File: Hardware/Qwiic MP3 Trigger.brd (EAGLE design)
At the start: 25.4 x 50.8 mm, 106 parts, among them J14 MICRO-SD, J2 QWIIC_RIGHT_ANGLE, J3 PTH, J4 QWIIC_RIGHT_ANGLE, J7 ISP, J8 3.5mm Audio, J9 Poke-Home, U1 TPA2005D1, U2 MY1690-16S, U3 AP2112-3.3V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

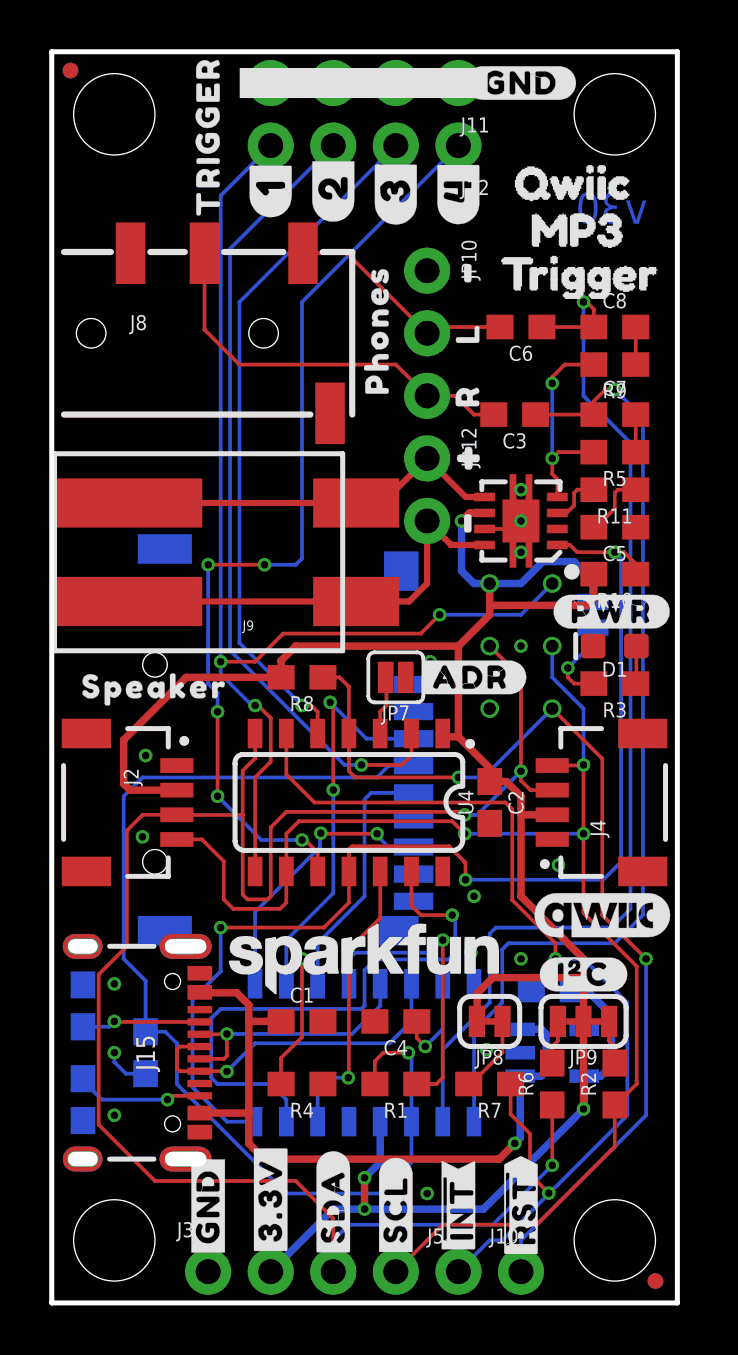
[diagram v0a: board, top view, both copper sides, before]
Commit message: Route MY1690X-16S
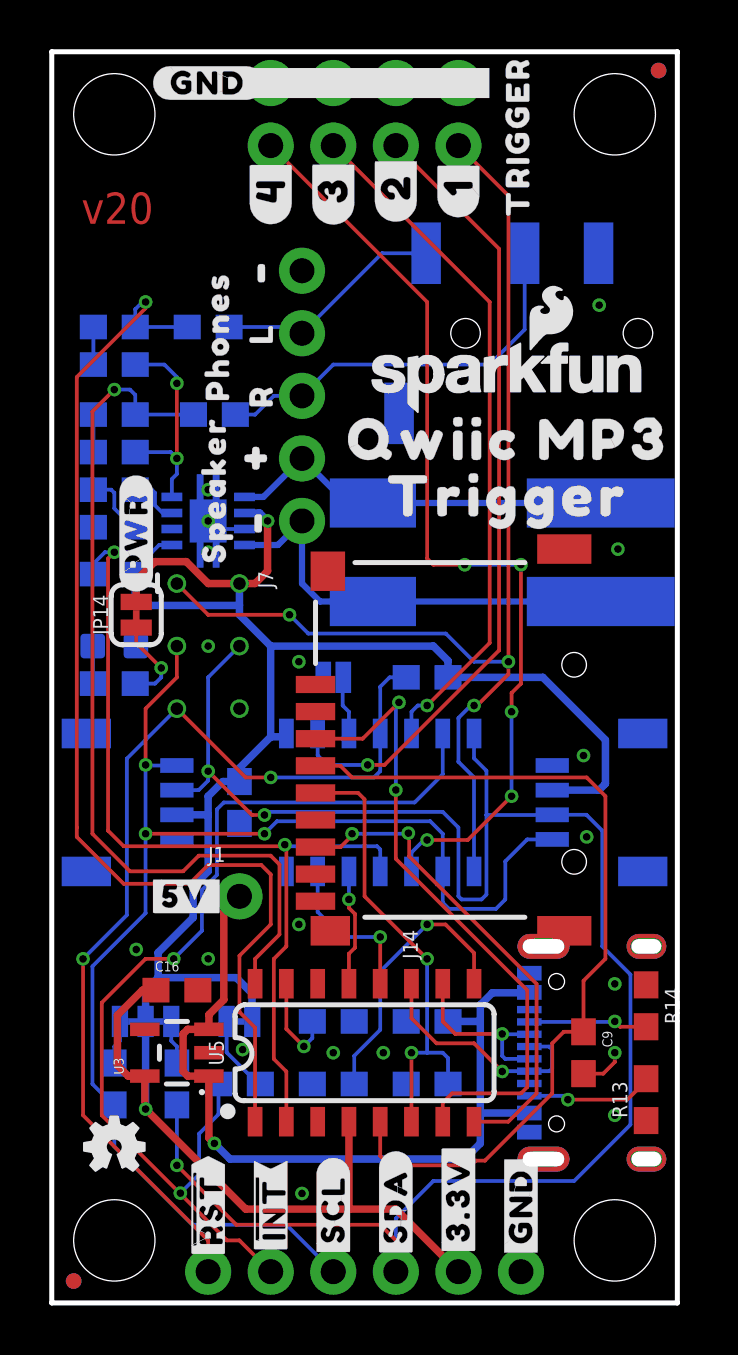
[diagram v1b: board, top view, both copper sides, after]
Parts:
- removed R1: 10k, SparkFun-Resistors:0603
- removed U2: MY1690-16S, MY1690:SO16
- added C10: 2.2uF, SparkFun-Capacitors:0603
- added J1: (no value), SparkFun-Connectors:1X01_NO_SILK
- added U$3: (no value), output:#5V#0
- added U5: MY1690X-16S, MY1690X-16S:SO16
- C4: value 1.0uF -> 2.2uF
- moved FRAME1 63.5 mm to (-19.1, -34.3), flipped to the top
- moved J8 25.4 mm to (25.4, 39.4), flipped to the bottom
- moved JP1 23.9 mm to (24.6, 50.0), flipped to the top
- moved JP6 23.9 mm to (24.6, 50.0), flipped to the bottom
- moved JP2 23.6 mm to (0.89, 0.89), flipped to the bottom
- moved JP5 23.6 mm to (0.89, 0.89), flipped to the top
- moved R13 22.9 mm to (24.1, 8.26), flipped to the top
- moved R14 22.9 mm to (24.1, 12.1), flipped to the top
- moved C5 20.3 mm to (2.54, 31.5), flipped to the bottom
- moved C7 20.3 mm to (2.54, 36.1), flipped to the bottom
- moved C8 20.3 mm to (2.54, 39.6), flipped to the bottom
- moved D1 20.3 mm to (2.54, 26.7), flipped to the bottom
- moved JP11 20.3 mm to (22.9, 2.54), flipped to the bottom
- moved JP13 20.3 mm to (2.54, 2.54), flipped to the bottom
- moved JP3 20.3 mm to (22.9, 48.3), flipped to the bottom
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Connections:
- removed net ADKEY: R1.1, U2.4
- new net N$10: C10.1, U5.9
- net 3.3V: now also U5.4; no longer U2.12
- net 5V: now also J1.1
- net D+: now also U5.11; no longer U2.6
- net D-: now also U5.10; no longer U2.5
- net GND: now also C10.2, U5.14, U5.3; no longer U2.13, U2.8
- net MP3-RXI: now also U5.12; no longer U2.15
- net MP3-TXO: now also U5.13; no longer U2.14
- net N$7: now also U5.15; no longer U2.7
- net PLAYING: now also U5.2; no longer U2.16
- net SD_CLK: now also U5.6; no longer U2.3
- net SD_CMD: now also U5.7; no longer U2.2
- net SD_DAT: now also U5.8; no longer U2.1
- net VCCIO: now also U5.5; no longer R1.2, U2.11
- net VOUTL: now also U5.16; no longer U2.9
- net VOUTR: now also U5.1; no longer U2.10
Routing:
- net MP3-RXI: track 23.4 -> 6.50 mm
- net ADKEY: track 11.9 -> 0.00 mm, vias 1 -> 0
- net N$10: track 0.00 -> 11.3 mm, vias 0 -> 1
- net SD_CMD: track 16.3 -> 26.3 mm
- net VCCIO: track 44.1 -> 35.5 mm, vias 1 -> 0
- net SD_DAT: track 11.3 -> 19.8 mm
- net PLAYING: track 46.8 -> 39.3 mm, vias 3 -> 2
- net MP3-TXO: track 11.6 -> 4.76 mm
- net 5V: track 29.1 -> 35.0 mm
- net D+: track 13.7 -> 9.81 mm
- net D-: track 10.7 -> 7.30 mm
- net VOUTL: track 39.5 -> 36.4 mm
- net VOUTR: track 43.4 -> 46.2 mm
- net SD_CLK: track 16.4 -> 18.9 mm, vias 1 -> 2
- net 3.3V: track 93.1 -> 92.3 mm, vias 4 -> 2
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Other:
- board text added: "v20"
- board text removed: "v30"

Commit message: Add v20 panel
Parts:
- moved FRAME1 63.5 mm to (44.5, -34.3), flipped to the bottom
- moved J8 25.4 mm to (0.00, 39.4), flipped to the top
- moved JP1 23.9 mm to (0.76, 50.0), flipped to the bottom
- moved JP6 23.9 mm to (0.76, 50.0), flipped to the top
- moved JP2 23.6 mm to (24.5, 0.89), flipped to the top
- moved JP5 23.6 mm to (24.5, 0.89), flipped to the bottom
- moved R13 22.9 mm to (1.27, 8.26), flipped to the bottom
- moved R14 22.9 mm to (1.27, 12.1), flipped to the bottom
- moved C5 20.3 mm to (22.9, 31.5), flipped to the top
- moved C7 20.3 mm to (22.9, 36.1), flipped to the top
- moved C8 20.3 mm to (22.9, 39.6), flipped to the top
- moved D1 20.3 mm to (22.9, 26.7), flipped to the top
- moved JP11 20.3 mm to (2.54, 2.54), flipped to the top
- moved JP13 20.3 mm to (22.9, 2.54), flipped to the top
- moved JP3 20.3 mm to (2.54, 48.3), flipped to the top
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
